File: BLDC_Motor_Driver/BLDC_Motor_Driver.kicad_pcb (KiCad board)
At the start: 4 copper layers, 225.6 x 150.2 mm, 132 parts, among them J101 Conn_01x10, J102 395221002, J103 USB4105-GF-A, J104 Conn_01x05, J105 Conn_01x05, J106 Conn_01x04, J107 395221005, J108 395221003, J109 Conn_02x12_Counter_Clockwise, J110 395221005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

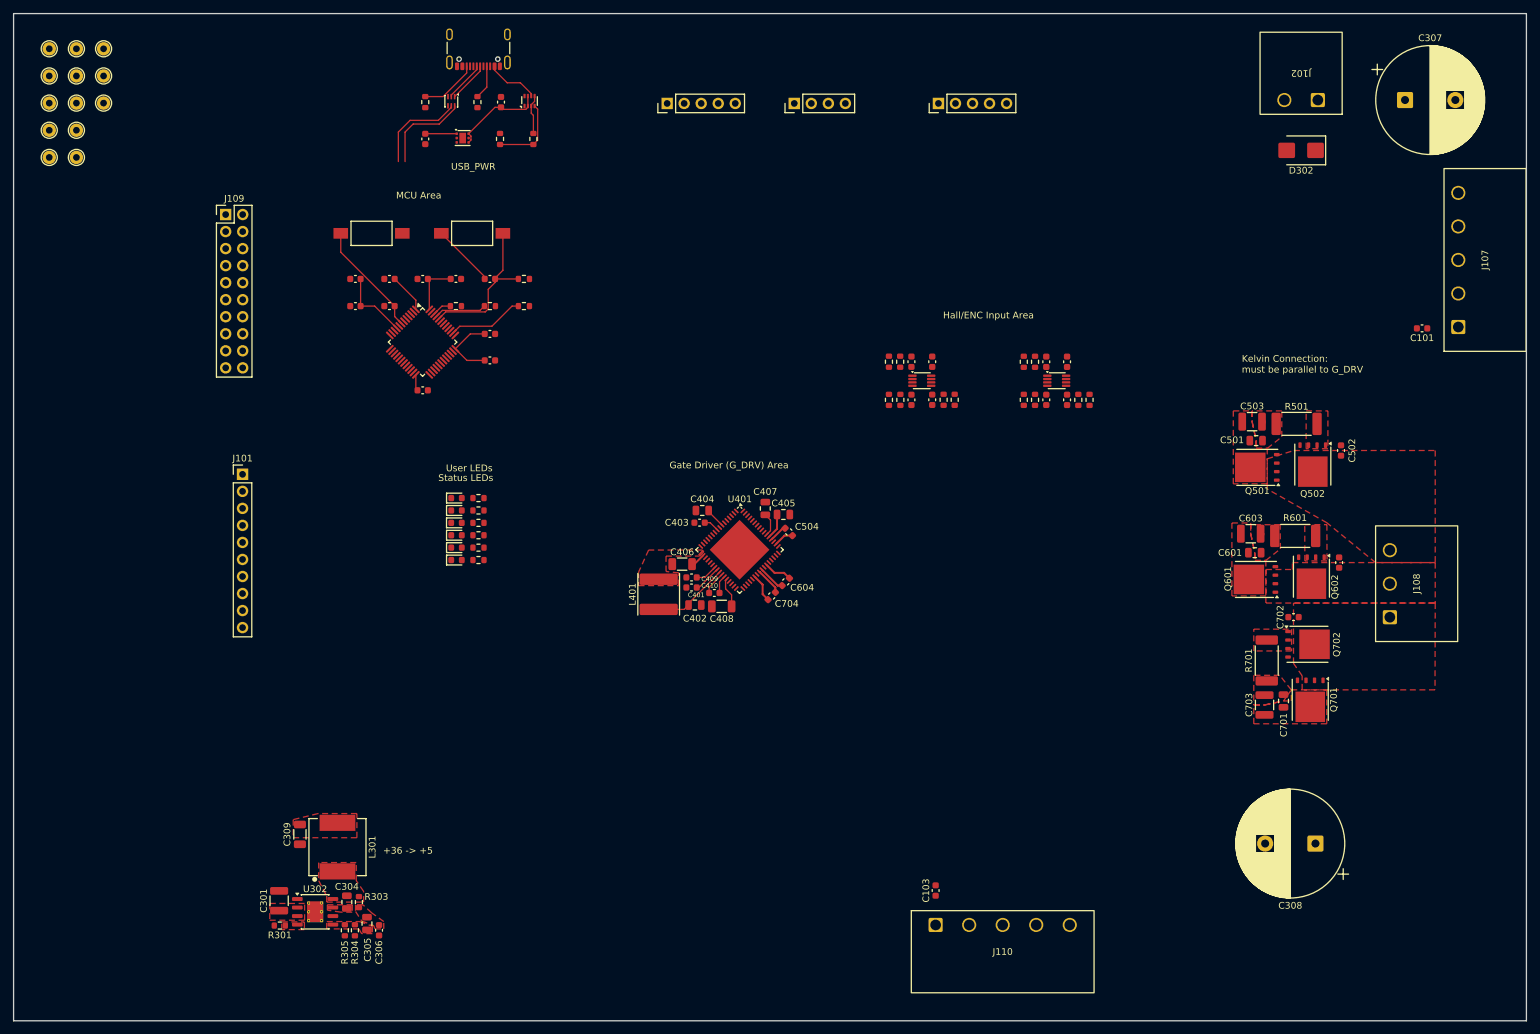
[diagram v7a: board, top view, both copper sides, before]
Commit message: board outline, most component placements, routed driver and some other stuff
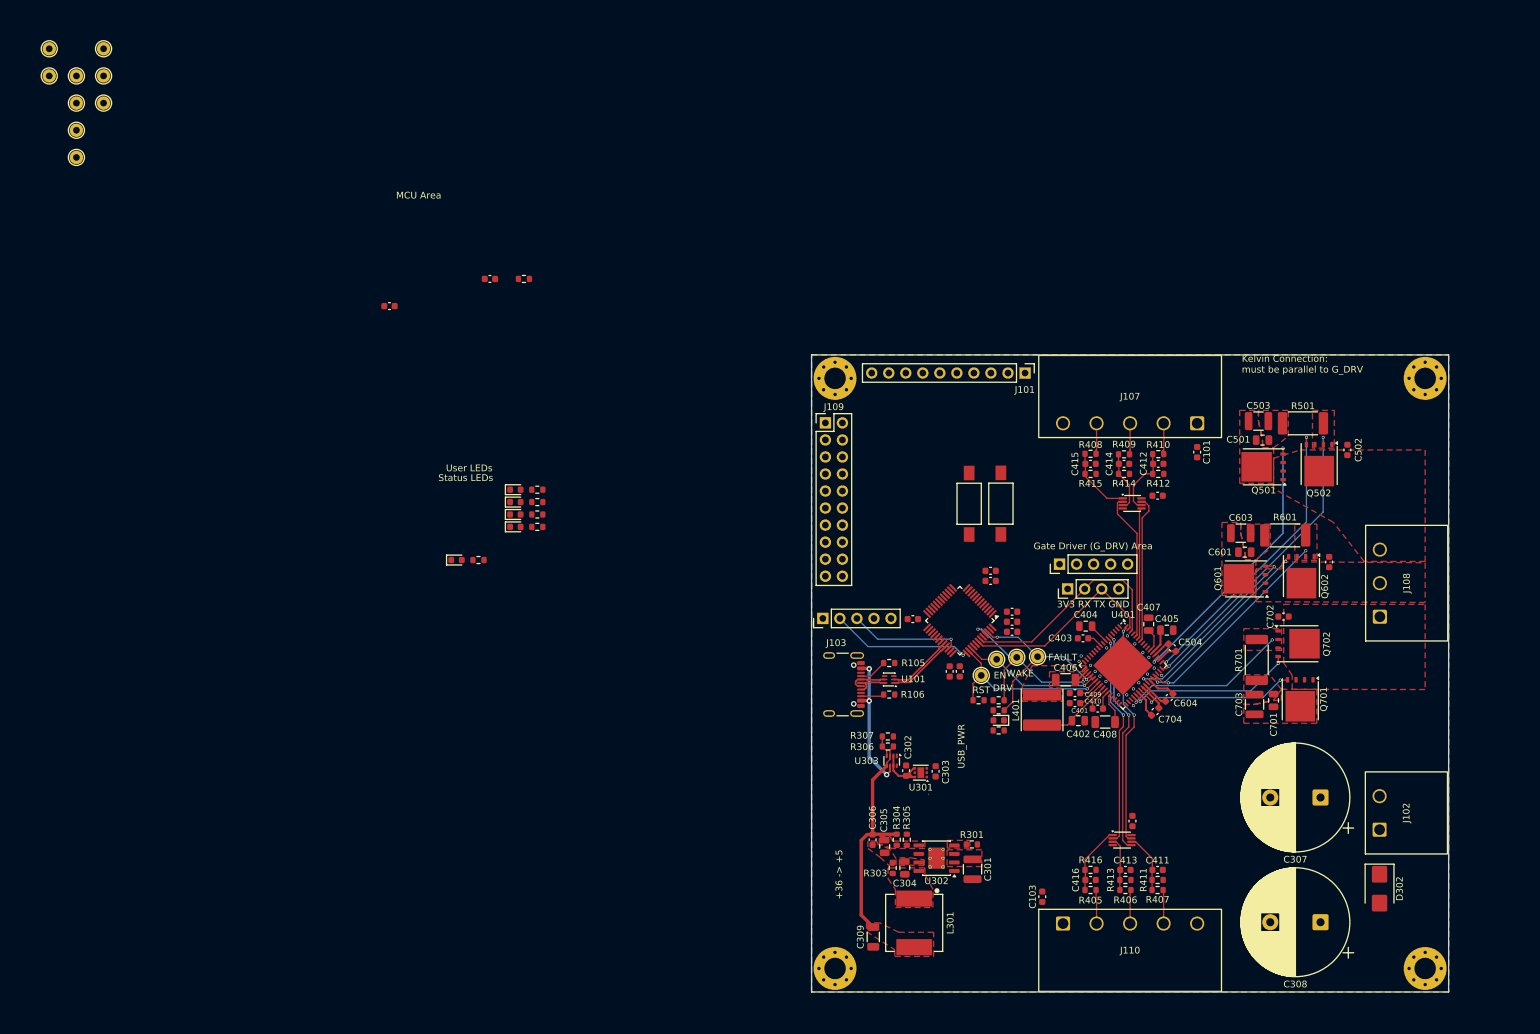
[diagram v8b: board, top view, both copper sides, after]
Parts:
- added H101: M3, MountingHole:MountingHole_3.2mm_M3_Pad_Via, F.Cu at (178.5, 68.5)
- added H102: M3, MountingHole:MountingHole_3.2mm_M3_Pad_Via, F.Cu at (266.5, 68.5)
- added H103: M3, MountingHole:MountingHole_3.2mm_M3_Pad_Via, F.Cu at (266.5, 156.5)
- added H104: M3, MountingHole:MountingHole_3.2mm_M3_Pad_Via, F.Cu at (178.5, 156.5)
- moved TP103 168.9 mm to (208.7, 110.0)
- moved TP106 167.0 mm to (205.6, 110.1)
- moved TP104 161.8 mm to (202.6, 110.4)
- moved TP105 159.0 mm to (200.3, 112.8)
- moved C303 121.2 mm to (193.5, 127.1), turned to 90 degrees
- moved J101 117.7 mm to (206.8, 67.7), turned to -90 degrees
- moved U301 116.7 mm to (191.3, 127.3), turned to 180 degrees
- moved C302 116.6 mm to (189.1, 127.0)
- moved U303 112.2 mm to (186.9, 125.5), turned to -90 degrees
- moved R106 112.2 mm to (186.6, 115.7), turned to 0 degrees
- moved D302 110.7 mm to (259.7, 144.6), turned to -90 degrees
- moved J103 109.7 mm to (178.7, 114.2), turned to -90 degrees
- moved J102 109.2 mm to (259.7, 135.8), turned to 90 degrees
- moved U101 108.2 mm to (186.6, 113.4), turned to 180 degrees
- moved R307 106.2 mm to (186.4, 121.9), turned to 0 degrees
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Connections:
- J106 pad 2: /USART1_TX -> /USART1_RX
- J106 pad 3: /USART1_RX -> /USART1_TX
- U101 pad 1: /D+ -> /USB_D+
- U101 pad 2: /D- -> /USB_D-
- U101 pad 5: /USB_D- -> /D-
- U101 pad 6: /USB_D+ -> /D+
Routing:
- net +3V3: track 54.0 -> 2.33 mm
- net /Gate-Driver/CSP_U: track 0.00 -> 44.9 mm, vias 0 -> 2
- net /Gate-Driver/LS_U: track 0.00 -> 43.9 mm, vias 0 -> 2
- net /Gate-Driver/HS_U: track 0.00 -> 41.6 mm, vias 0 -> 2
- net /Gate-Driver/ENC_B: track 0.00 -> 33.6 mm, vias 0 -> 2
- net /Gate-Driver/ENC_A/TXEN: track 0.00 -> 33.5 mm, vias 0 -> 2
- net /USART1_RX: track 0.00 -> 33.4 mm
- net /Gate-Driver/ENC_N: track 0.00 -> 31.8 mm, vias 0 -> 2
- net /Gate-Driver/CSP_V: track 0.00 -> 31.1 mm, vias 0 -> 2
- net /USART1_TX: track 0.00 -> 30.0 mm
- net /Gate-Driver/HS_V: track 0.00 -> 28.6 mm, vias 0 -> 2
- net /Gate-Driver/LS_V: track 0.00 -> 28.5 mm, vias 0 -> 2
- net /5V_REG: track 5.91 -> 33.8 mm
- net /DRIVER_FAULTN: track 2.93 -> 28.7 mm, vias 0 -> 2
- net /Gate-Driver/LS_W: track 0.00 -> 25.3 mm, vias 0 -> 2
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- added copper zone on B.Cu, net GND
- added copper zone on In1.Cu, net GND
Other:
- board size 225.6 x 150.2 mm -> 95 x 95 mm
- board text added: "3V3 RX TX GND"
- board text added: "DRV"
- board text added: "EN"
- board text added: "FAULT"
- board text added: "RST"
- board text added: "WAKE"
- board text removed: "Hall/ENC Input Area"
